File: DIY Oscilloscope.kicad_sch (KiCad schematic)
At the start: 2 parts, among them J1 Conn_Coaxial, U3 STM32F401RETx

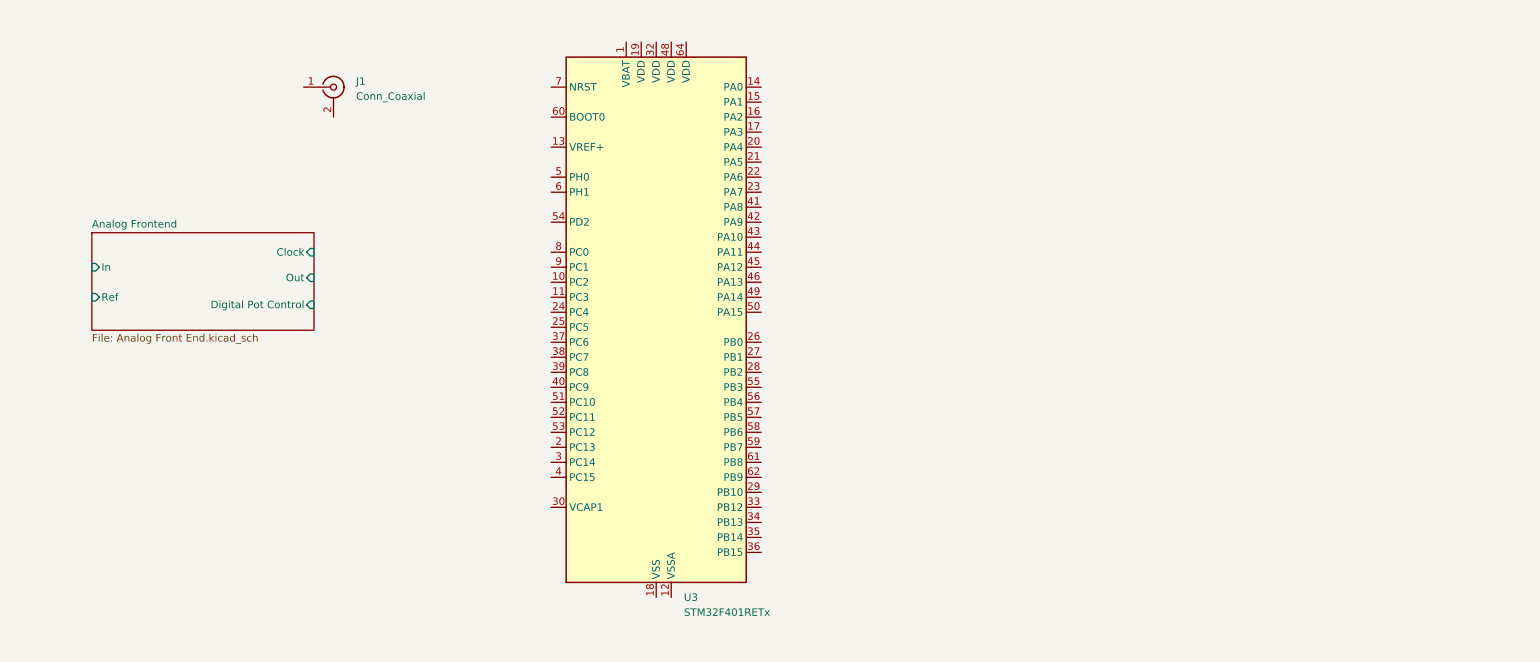
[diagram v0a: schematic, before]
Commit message: fixed 10x voltage divider
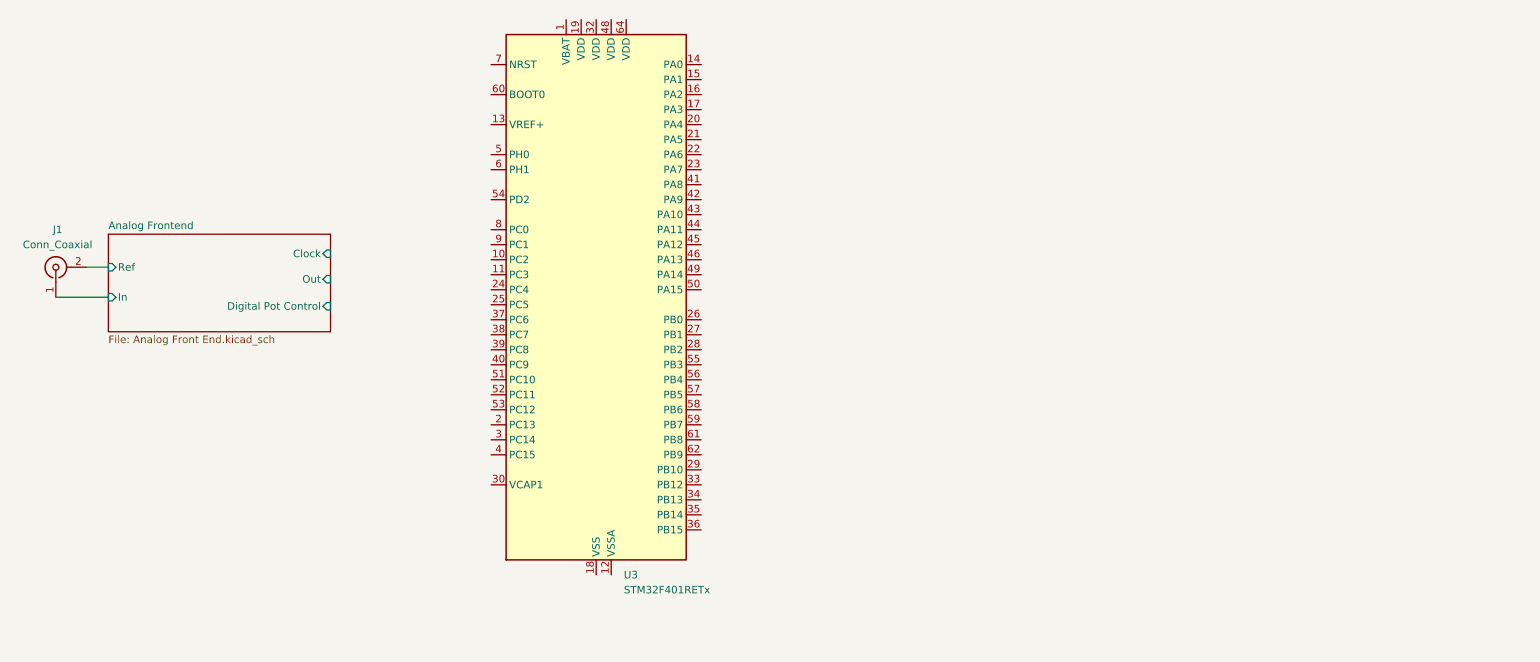
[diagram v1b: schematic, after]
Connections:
- net Analog Frontend/In: now also J1.1 (In)
- net Analog Frontend/Ref: now also J1.2 (Ext)
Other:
- moved on the sheet: J1, U3
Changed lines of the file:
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@@
 	(generator_version "10.0")
 	(paper "A4")
+	(wire
+		(pts
+			(xy 39.37 66.04) (xy 43.18 66.04)
+		)
+		(stroke
+			(width 0)
+			(type default)
+		)
+	)
+	(wire
+		(pts
+			(xy 34.29 71.12) (xy 43.18 71.12)
+		)
+		(stroke
+			(width 0)
+			(type default)
+		)
+	)
 	(symbol
 		(lib_id "MCU_ST_STM32F4:STM32F401RETx")
-		(at 135.89 76.2 0)
+		(at 125.73 72.39 0)
 		(unit 1)
 		(body_style 1)
@@
 		(fields_autoplaced yes)
 		(property "Reference" "U3"
-			(at 140.5733 121.92 0)
+			(at 130.4133 118.11 0)
 			(show_name no)
 			(do_not_autoplace no)
@@
 		)
 		(property "Value" "STM32F401RETx"
-			(at 140.5733 124.46 0)
+			(at 130.4133 120.65 0)
 			(show_name no)
 			(do_not_autoplace no)
@@
 		)
 		(property "Footprint" "Package_QFP:LQFP-64_10x10mm_P0.5mm"
-			(at 120.65 119.38 0)
+			(at 110.49 115.57 0)
 			(hide yes)
 			(show_name no)
@@
 		)
 		(property "Datasheet" "https://www.st.com/resource/en/datasheet/stm32f401re.pdf"
-			(at 135.89 76.2 0)
+			(at 125.73 72.39 0)
 			(hide yes)
 			(show_name no)
@@
 		)
 		(property "Description" "STMicroelectronics Arm Cortex-M4 MCU, 512KB flash, 96KB RAM, 84 MHz, 1.7-3.6V, 50 GPIO, LQFP64"
-			(at 135.89 76.2 0)
+			(at 125.73 72.39 0)
 			(hide yes)
 			(show_name no)
@@
 	(symbol
 		(lib_id "Connector:Conn_Coaxial")
-		(at 81.28 35.56 0)
+		(at 34.29 66.04 90)
 		(unit 1)
 		(body_style 1)
@@
 		(fields_autoplaced yes)
 		(property "Reference" "J1"
-			(at 85.09 34.5831 0)
-			(show_name no)
-			(do_not_autoplace no)
-			(effects
-				(font
-					(size 1.27 1.27)
-				)
-				(justify left)
+			(at 34.5832 59.69 90)
+			(show_name no)
+			(do_not_autoplace no)
+			(effects
+				(font
+					(size 1.27 1.27)
+				)
 			)
 		)
 		(property "Value" "Conn_Coaxial"
-			(at 85.09 37.1231 0)
-			(show_name no)
-			(do_not_autoplace no)
-			(effects
-				(font
-					(size 1.27 1.27)
-				)
-				(justify left)
+			(at 34.5832 62.23 90)
+			(show_name no)
+			(do_not_autoplace no)
+			(effects
+				(font
+					(size 1.27 1.27)
+				)
 			)
 		)
 		(property "Footprint" ""
-			(at 81.28 35.56 0)
+			(at 34.29 66.04 0)
 			(hide yes)
 			(show_name no)
@@
 		)
 		(property "Datasheet" ""
-			(at 81.28 35.56 0)
+			(at 34.29 66.04 0)
 			(hide yes)
 			(show_name no)
@@
 		)
 		(property "Description" "coaxial connector (BNC, SMA, SMB, SMC, Cinch/RCA, LEMO, ...)"
-			(at 81.28 35.56 0)
+			(at 34.29 66.04 0)
 			(hide yes)
 			(show_name no)
@@
 	)
 	(sheet
-		(at 40.386 60.198)
+		(at 43.18 60.452)
 		(size 37.592 16.51)
 		(exclude_from_sim no)
@@
 		)
 		(property "Sheetname" "Analog Frontend"
-			(at 40.386 59.4864 0)
+			(at 43.18 59.7404 0)
 			(show_name no)
 			(do_not_autoplace no)
@@
 		)
 		(property "Sheetfile" "Analog Front End.kicad_sch"
-			(at 40.386 77.2926 0)
+			(at 43.18 77.5466 0)
 			(show_name no)
 			(do_not_autoplace no)
@@
 		)
 		(pin "Clock" input
-			(at 77.978 63.5 0)
+			(at 80.772 63.754 0)
 			(effects
 				(font
@@
 		)
 		(pin "Digital Pot Control" input
-			(at 77.978 72.39 0)
+			(at 80.772 72.644 0)
 			(effects
 				(font
@@
 		)
 		(pin "In" input
-			(at 40.386 66.04 180)
+			(at 43.18 71.12 180)
 			(effects
 				(font
@@
 		)
 		(pin "Out" input
-			(at 77.978 67.818 0)
+			(at 80.772 68.072 0)
 			(effects
 				(font
@@
 		)
 		(pin "Ref" input
-			(at 40.386 71.12 180)
-			(effects
-				(font
+			(at 43.18 66.04 180)
+			(effects
+				(font

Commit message: added MCU, crystal, and USB-C port
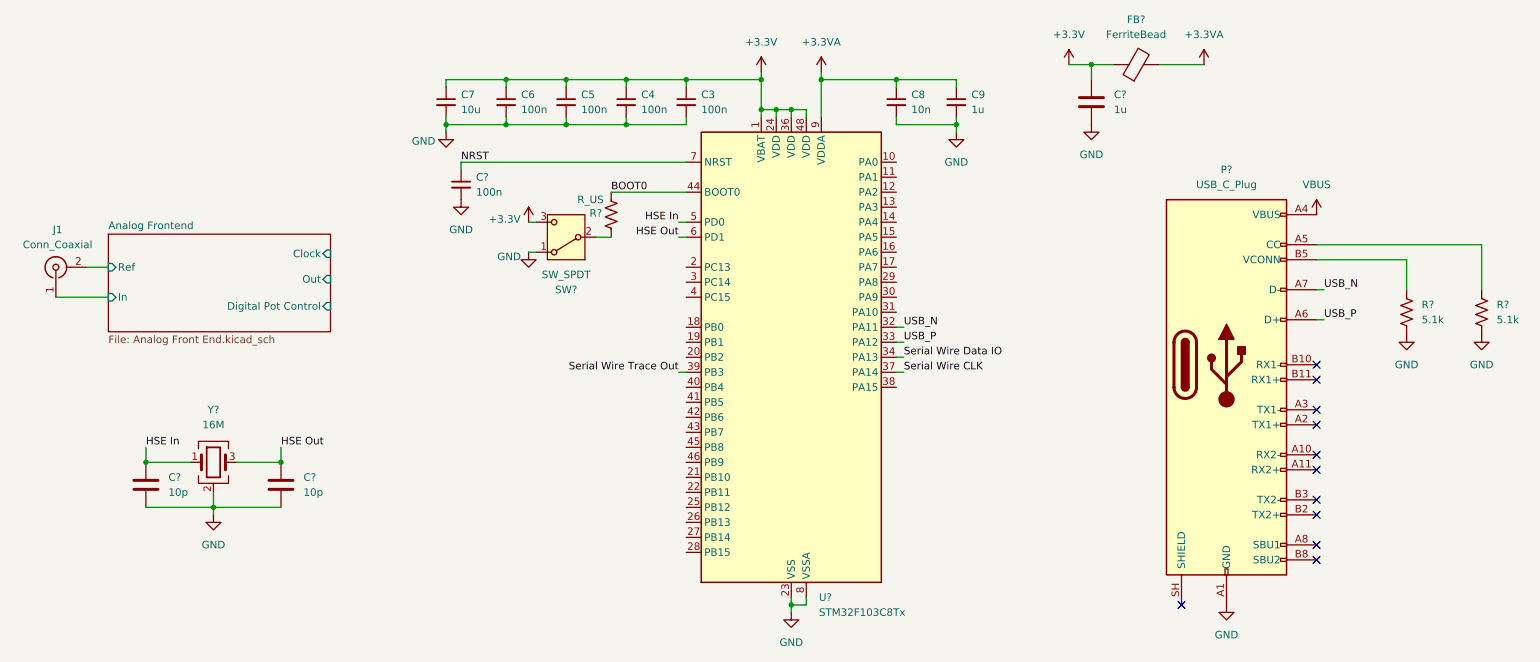
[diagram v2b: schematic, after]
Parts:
- removed U3: STM32F401RETx, Package_QFP:LQFP-64_10x10mm_P0.5mm, symbol MCU_ST_STM32F4:STM32F401RETx
- added C3, C4, C5, C6, C?: 100n, symbol Device:C_Small
- added C7: 10u, symbol Device:C_Small
- added C8: 10n, symbol Device:C_Small
- added C9: 1u, symbol Device:C_Small
- added C? (x2): 10p, symbol Device:C
- added C?: 1u, symbol Device:C
- added FB?: FerriteBead, symbol Device:FerriteBead
- added P?: USB_C_Plug, symbol Connector:USB_C_Plug
- added R? (x2): 5.1k, symbol Device:R_US
- added R?: R_US, symbol Device:R_US
- added SW?: SW_SPDT, symbol Switch:SW_SPDT
- added U?: STM32F103C8Tx, Package_QFP:LQFP-48_7x7mm_P0.5mm, symbol MCU_ST_STM32F1:STM32F103C8Tx
- added Y?: 16M, symbol Device:Crystal_GND24
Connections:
- new net: P?.B5 (VCONN), R?.1
- new net: P?.A5 (CC), R?.1
- new net: R?.2, SW?.2 (B)
- new net +3.3V: C3.1, C4.1, C5.1, C6.1, C7.1, C?.1, FB?.1, SW?.3 (C), U?.1 (VBAT), U?.24 (VDD), U?.36 (VDD), U?.48 (VDD)
- new net +3.3VA: C8.1, C9.1, FB?.2, U?.9 (VDDA)
- new net BOOT0: R?.1, U?.44 (BOOT0)
- new net GND: C3.2, C4.2, C5.2, C6.2, C7.2, C8.2, C9.2, C?.2, C?.2, C?.2, C?.2, P?.A1 (GND), P?.A12 (GND), P?.B1 (GND), P?.B12 (GND), R?.2, R?.2, SW?.1 (A), U?.23 (VSS), U?.35 (VSS), U?.47 (VSS), U?.8 (VSSA), Y?.2 (G), Y?.4 (G)
- new net HSE In: C?.1, U?.5 (PD0), Y?.1
- new net HSE Out: C?.1, U?.6 (PD1), Y?.3
- new net NRST: C?.1, U?.7 (NRST)
- new net Serial Wire CLK: U?.37 (PA14)
- new net Serial Wire Data IO: U?.34 (PA13)
- new net Serial Wire Trace Out: U?.39 (PB3)
- new net USB_N: P?.A7 (D-), U?.32 (PA11)
- new net USB_P: P?.A6 (D+), U?.33 (PA12)
- new net VBUS: P?.A4 (VBUS), P?.A9 (VBUS), P?.B4 (VBUS), P?.B9 (VBUS)
- no-connect marks 0 -> 11
